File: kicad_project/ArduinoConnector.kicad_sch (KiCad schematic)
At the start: 12 parts, among them J5 1x8, J6 1x6, J7 1x10, J8 1x8

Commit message: Fix some missing silkscreen labels
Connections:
- net GPIN2: now reaches J8.2 (Pin_2), R1.1
- net GPIN1: now reaches J8.4 (Pin_4), R1.1
- net GPIN0: now reaches J8.6 (Pin_6), R1.1
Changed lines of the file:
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@@
     (effects (font (size 1.27 1.27)) (justify right bottom))
+  )
+  (label "GPIN0" (at 181.61 110.49 0) (fields_autoplaced)
+    (effects (font (size 1.27 1.27)) (justify left bottom))
   )
   (label "SPI.MISO" (at 181.61 72.39 0) (fields_autoplaced)
@@
     (effects (font (size 1.27 1.27)) (justify left bottom))
   )
+  (label "GPIN1" (at 181.61 105.41 0) (fields_autoplaced)
+    (effects (font (size 1.27 1.27)) (justify left bottom))
+  )
   (label "PWM_OUT" (at 228.6 102.87 0) (fields_autoplaced)
     (effects (font (size 1.27 1.27)) (justify left bottom))
@@
     (effects (font (size 1.27 1.27)) (justify right bottom))
   )
+  (label "GPIN2" (at 181.61 100.33 0) (fields_autoplaced)
+    (effects (font (size 1.27 1.27)) (justify left bottom))
+  )
   (label "GPOUT0" (at 181.61 107.95 0) (fields_autoplaced)

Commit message: Update to KiCAD 8, start adding CAN transceiver
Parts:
- renumbered C9 to C36, J8 to J4, NT1 to NT10, NT1 to NT11, NT1 to NT9, R1 to R27, R1 to R28, R1 to R30, R1 to R31

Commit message: Fix all known issues with v2 r2: * Invert polarity of SD card enable line to match power switch * Decrease SPI mirror resistor resistance * Pull up SD card MISO line to 3V3 * Fix reset voltage divider to output 3.3V instead of 4V * Add diode to keep reset low while power is unplugged * Move analog in to A3 instead of A0
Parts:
- removed C36: 1u, Capacitor_SMD:C_1206_3216Metric, symbol Device:C_Small
- removed R31: 1.5k, Resistor_SMD:R_1206_3216Metric, symbol Device:R_US
- added C26: 1u, Capacitor_SMD:C_1206_3216Metric, symbol Device:C_Small
- added R29: 1.5k, Resistor_SMD:R_1206_3216Metric, symbol Device:R_US
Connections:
- net ANALOG_IN: now also J6.3 (Pin_3), C26.2, R29.1; no longer J6.1 (Pin_1)
- net GND: now also C26.1
- net PWM_OUT: now also R29.2
- net SD_CARD_ENABLE renamed ~SD_CARD_ENABLE

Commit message: Start adding CAN support... ~75% done with schematics
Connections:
- net SPI.SD_CS renamed SPI.CAN_SD_CS
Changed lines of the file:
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@@
 		)
 	)
-	(text_box "SPI has 2 chip selects:\n* SD_CS goes to the SD card socket.  It's monitored by the logic analyzer but not hooked to the CY7C65211.  This can be any GPIO pin since the SD card driver does not work with HW CS anyway\n* HW_CS is used for master-mode SPI operations to the logic analyzer, and also slave-mode SPI operations with the CY7C65211 as the master.  Since slave mode usually only works with a hardware CS pin, HW_CS should be connected to a hardware CS pin if available."
+	(text_box "SPI has 2 chip selects:\n* CAN_SD_CS goes to the SD card socket or the CAN transceiver (depending on the SD card enable line).  It's monitored by the logic analyzer but not hooked to the CY7C65211.  This can be any GPIO pin since the SD card driver does not work with HW CS anyway\n* HW_CS is used for master-mode SPI operations to the logic analyzer, and also slave-mode SPI operations with the CY7C65211 as the master.  Since slave mode usually only works with a hardware CS pin, HW_CS should be connected to a hardware CS pin if available."
 		(exclude_from_sim no)
 		(at 223.52 49.53 0)
@@
 		)
 	)
-	(label "SPI.SD_CS"
+	(label "SPI.CAN_SD_CS"
 		(at 181.61 82.55 0)
 		(effects
@@
 		)
 	)
-	(hierarchical_label "SPI{SCLK MOSI MISO SD_CS HW_CS}"
+	(hierarchical_label "SPI{SCLK MOSI MISO CAN_SD_CS HW_CS}"
 		(shape bidirectional)
 		(at 212.09 59.69 90)
@@
 			)
 		)
-		(property "Description" ""
+		(property "Description" "Power symbol creates a global label with name \"GND\" , ground"
 			(at 83.82 113.03 0)
 			(effects
@@
 			)
 		)
-		(property "Description" ""
+		(property "Description" "Power symbol creates a global label with name \"GND\" , ground"
 			(at 198.12 86.36 0)
 			(effects
@@
 			)
 		)
-		(property "Description" ""
+		(property "Description" "Power symbol creates a global label with name \"GND\" , ground"
 			(at 119.38 85.09 0)
 			(effects

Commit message: ERC passing!
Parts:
- removed NT11: NetTie_2, NetTie:NetTie-2_SMD_Pad0.5mm, symbol Device:NetTie_2
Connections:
- net ~SD_CARD_ENABLE renamed SD_CARD_ENABLE

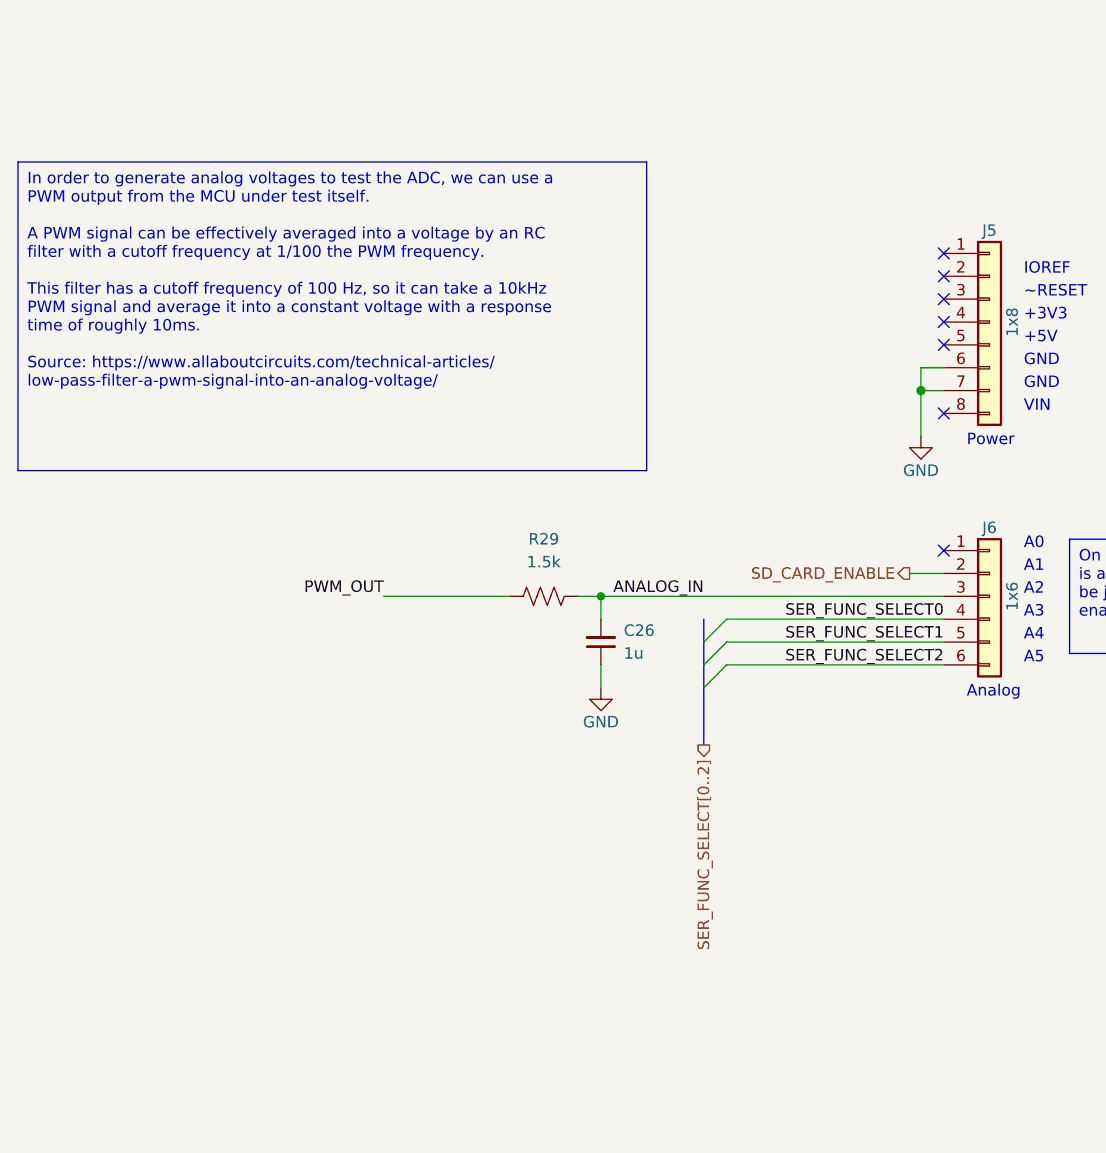
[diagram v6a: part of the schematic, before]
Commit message: Finish new SD card schematic, ERC passing!
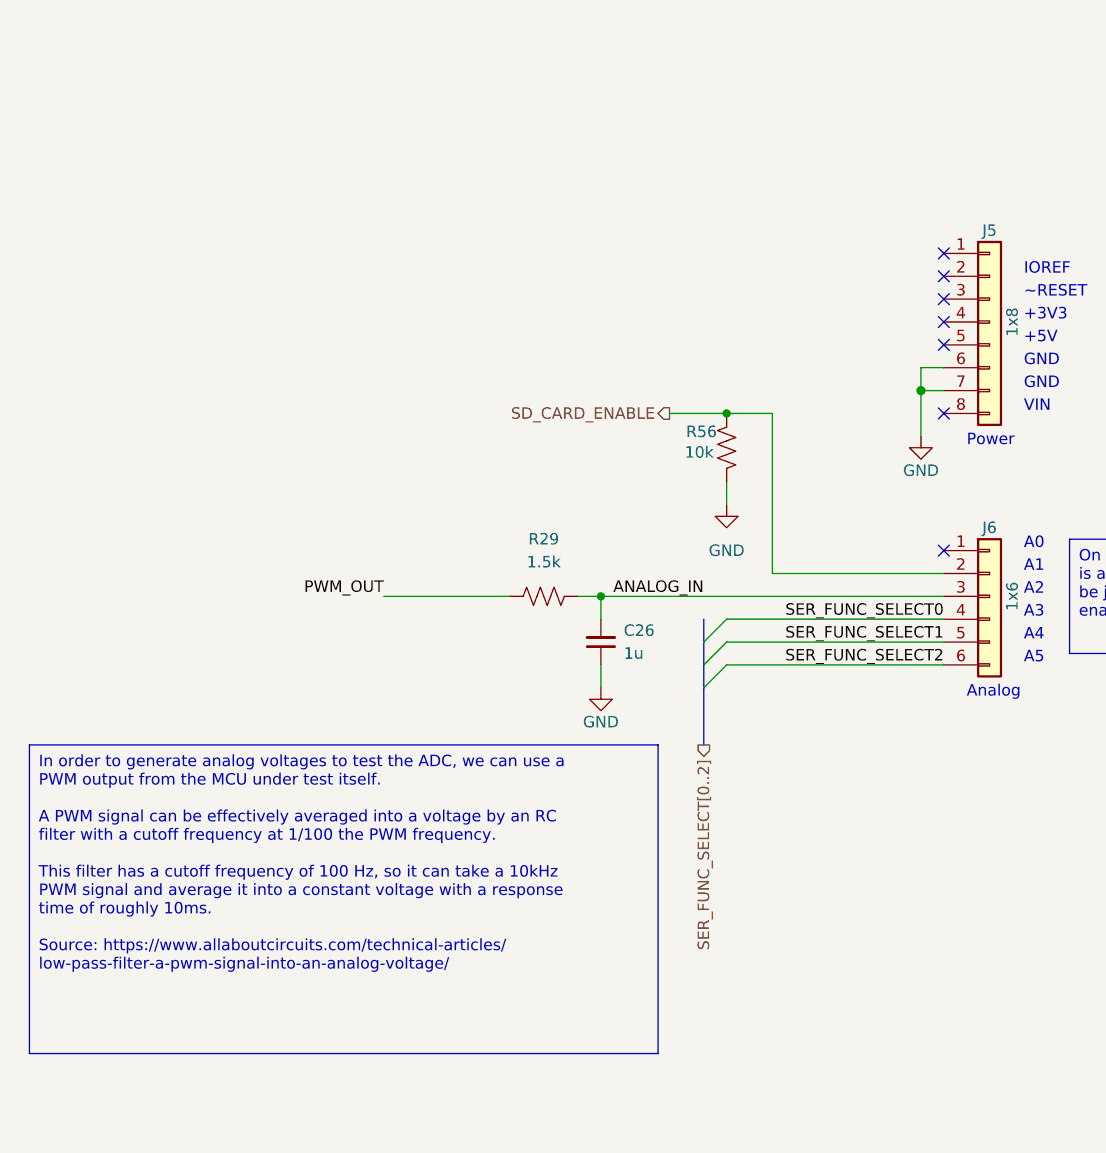
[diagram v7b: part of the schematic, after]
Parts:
- added R56: 10k, Resistor_SMD:R_1206_3216Metric, symbol Device:R_US
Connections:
- net GND: now also R56.1
- net SD_CARD_ENABLE: now also R56.2
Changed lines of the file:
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@@
+	)
+	(junction
+		(at 97.79 82.55)
+		(diameter 0)
+		(color 0 0 0 0)
 	)
 	(junction
@@
 	(wire
 		(pts
+			(xy 102.87 100.33) (xy 121.92 100.33)
+		)
+		(stroke
+			(width 0)
+			(type default)
+		)
+	)
+	(wire
+		(pts
 			(xy 181.61 82.55) (xy 209.55 82.55)
 		)
@@
 	(wire
 		(pts
-			(xy 118.11 100.33) (xy 121.92 100.33)
+			(xy 91.44 82.55) (xy 97.79 82.55)
 		)
 		(stroke
@@
 		)
 	)
+	(wire
+		(pts
+			(xy 97.79 90.17) (xy 97.79 92.71)
+		)
+		(stroke
+			(width 0)
+			(type default)
+		)
+	)
 	(bus
 		(pts
@@
 		)
 	)
+	(wire
+		(pts
+			(xy 102.87 82.55) (xy 102.87 100.33)
+		)
+		(stroke
+			(width 0)
+			(type default)
+		)
+	)
 	(bus
 		(pts
 			(xy 240.03 115.57) (xy 240.03 118.11)
+		)
+		(stroke
+			(width 0)
+			(type default)
+		)
+	)
+	(wire
+		(pts
+			(xy 97.79 82.55) (xy 102.87 82.55)
 		)
 		(stroke
@@
 	(text_box "In order to generate analog voltages to test the ADC, we can use a PWM output from the MCU under test itself.\n\nA PWM signal can be effectively averaged into a voltage by an RC filter with a cutoff frequency at 1/100 the PWM frequency.\n\nThis filter has a cutoff frequency of 100 Hz, so it can take a 10kHz PWM signal and average it into a constant voltage with a response time of roughly 10ms.\n\nSource: https://www.allaboutcircuits.com/technical-articles/\nlow-pass-filter-a-pwm-signal-into-an-analog-voltage/"
 		(exclude_from_sim no)
-		(at 19.05 54.61 0)
+		(at 20.32 119.38 0)
 		(size 69.85 34.29)
 		(stroke
@@
 	(hierarchical_label "SD_CARD_ENABLE"
 		(shape output)
-		(at 118.11 100.33 180)
+		(at 91.44 82.55 180)
 		(effects
 			(font
@@
 	)
 	(symbol
+		(lib_id "Device:R_US")
+		(at 97.79 86.36 0)
+		(mirror x)
+		(unit 1)
+		(exclude_from_sim no)
+		(in_bom yes)
+		(on_board yes)
+		(dnp no)
+		(property "Reference" "R56"
+			(at 94.996 84.582 0)
+			(effects
+				(font
+					(size 1.27 1.27)
+				)
+			)
+		)
+		(property "Value" "10k"
+			(at 94.742 86.868 0)
+			(effects
+				(font
+					(size 1.27 1.27)
+				)
+			)
+		)
+		(property "Footprint" "Resistor_SMD:R_1206_3216Metric"
+			(at 98.806 86.106 90)
+			(effects
+				(font
+					(size 1.27 1.27)
+				)
+				(hide yes)
+			)
+		)
+		(property "Datasheet" "~"
+			(at 97.79 86.36 0)
+			(effects
+				(font
+					(size 1.27 1.27)
+				)
+				(hide yes)
+			)
+		)
+		(property "Description" "Resistor, US symbol"
+			(at 97.79 86.36 0)
+			(effects
+				(font
+					(size 1.27 1.27)
+				)
+				(hide yes)
+			)
+		)
+		(property "Supplier" "Digi-Key"
+			(at 97.79 86.36 0)
+			(effects
+				(font
+					(size 1.27 1.27)
+				)
+				(hide yes)
+			)
+		)
+		(property "LibRef" "ERJ-8ENF1002V"
+			(at 97.79 86.36 0)
+			(effects
+				(font
+					(size 1.27 1.27)
+				)
+				(hide yes)
+			)
+		)
+		(property "SKU" "P10.0KFCT-ND"
+			(at 97.79 86.36 0)
+			(effects
+				(font
+					(size 1.27 1.27)
+				)
+				(hide yes)
+			)
+		)
+		(pin "1"
+		)
+		(pin "2"
+		)
+		(instances
+			(project "mbed-ce-ci-shield-v2"
+				(path "/a0f40274-9469-4bcf-885c-e8b8a490ea54/1e471c6e-a872-4398-8c30-01f0a30d79ce"
+					(reference "R56")
+					(unit 1)
+				)
+			)
+		)
+	)
+	(symbol
 		(lib_id "power:GND")
 		(at 198.12 86.36 0)
@@
 					(unit 1)
 				)
+			)
+		)
+	)
+	(symbol
+		(lib_id "power:GND")
+		(at 97.79 92.71 0)
+		(unit 1)
+		(exclude_from_sim no)
+		(in_bom yes)
+		(on_board yes)
+		(dnp no)
+		(fields_autoplaced yes)
+		(property "Reference" "#PWR073"
+			(at 97.79 99.06 0)
+			(effects
+				(font
+					(size 1.27 1.27)
+				)
+				(hide yes)
+			)
+		)
+		(property "Value" "GND"
+			(at 97.79 97.79 0)
+			(effects
+				(font
+					(size 1.27 1.27)
+				)
+			)
+		)
+		(property "Footprint" ""
+			(at 97.79 92.71 0)
+			(effects
+				(font
+					(size 1.27 1.27)
+				)
+				(hide yes)
+			)
+		)
+		(property "Datasheet" ""
+			(at 97.79 92.71 0)
+			(effects
+				(font
+					(size 1.27 1.27)
+				)
+				(hide yes)
+			)
+		)
+		(property "Description" "Power symbol creates a global label with name \"GND\" , ground"
+			(at 97.79 92.71 0)
+			(effects
+				(font
+					(size 1.27 1.27)
+				)
+				(hide yes)
+			)
+		)
+		(pin "1"
+		)
+		(instances
+			(project "mbed-ce-ci-shield-v2"
+				(path "/a0f40274-9469-4bcf-885c-e8b8a490ea54/1e471c6e-a872-4398-8c30-01f0a30d79ce"
+					(reference "#PWR073")
+					(unit 1)
+				)

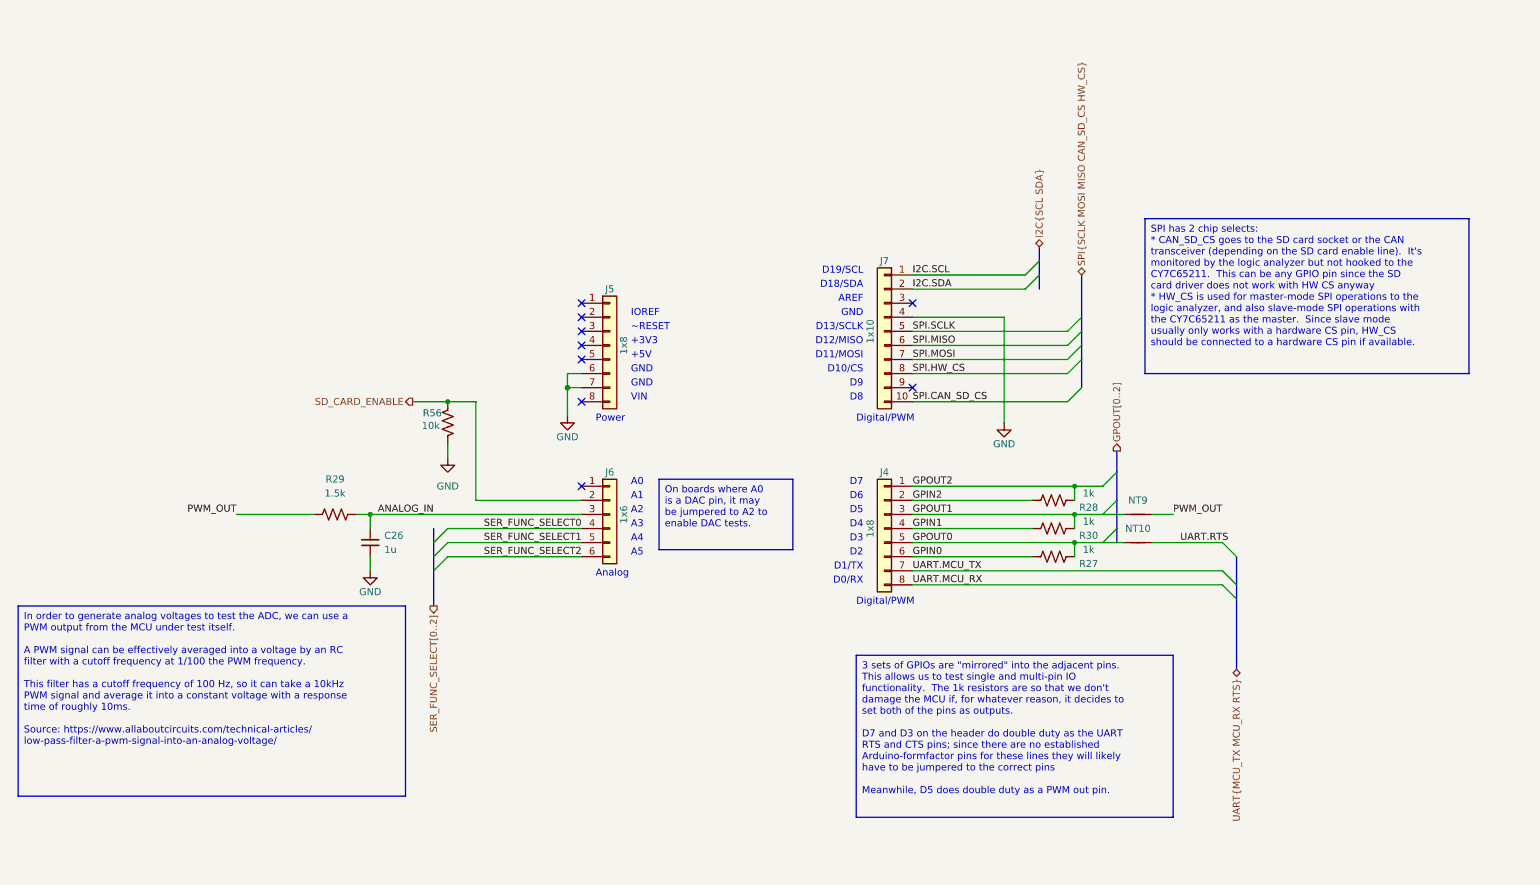
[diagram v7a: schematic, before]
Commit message: Switch out multiplexer, start switch FX2LP out for RP2040
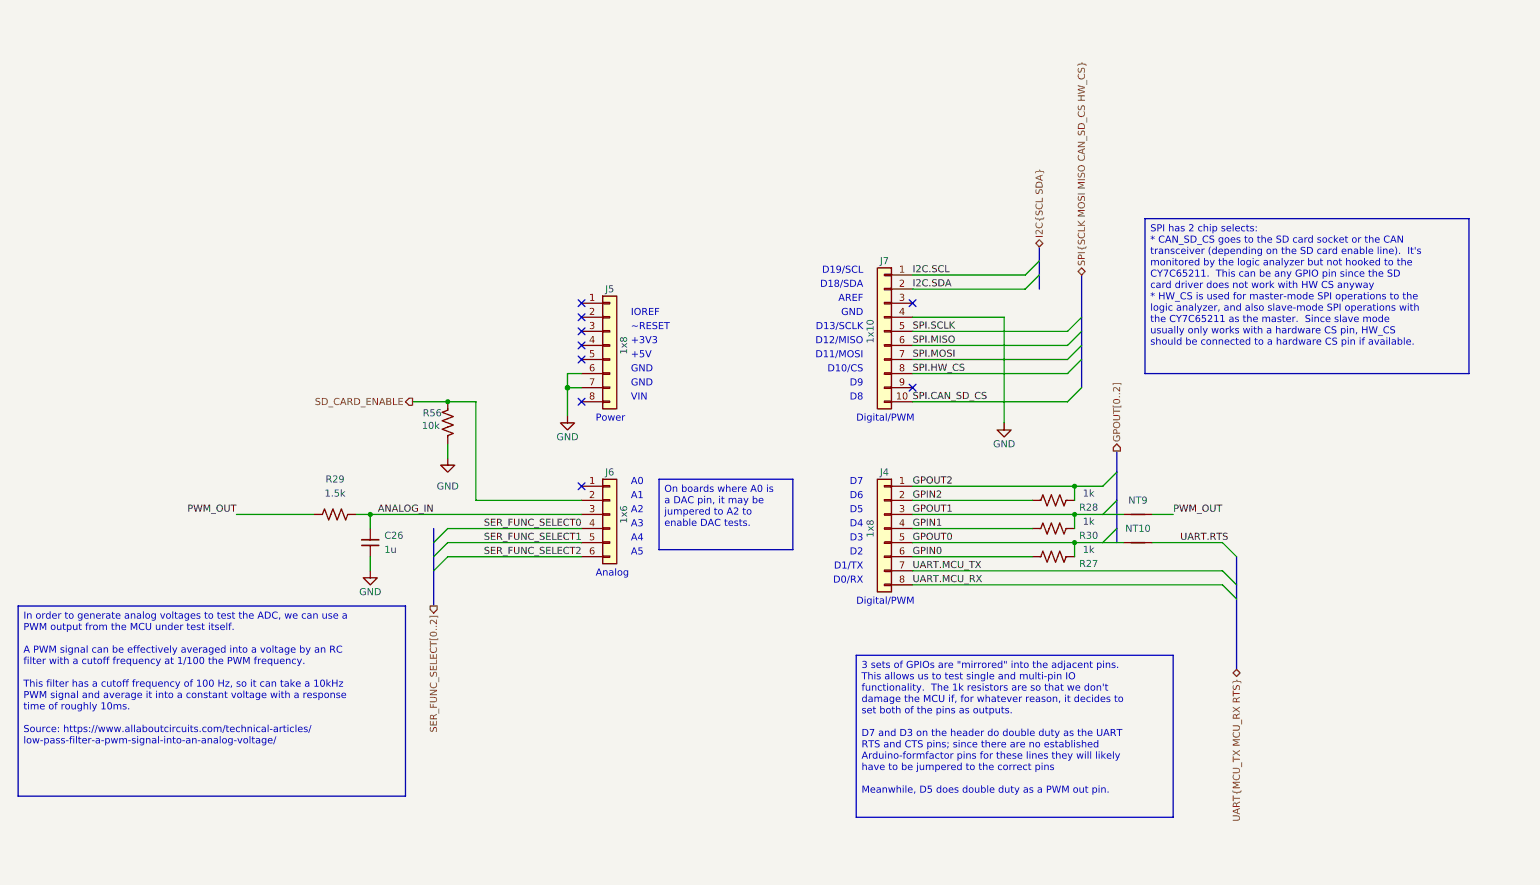
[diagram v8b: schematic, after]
